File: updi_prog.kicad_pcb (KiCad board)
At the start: 2 copper layers, 50 x 37 mm, 17 parts, among them J1 UPDI, P1 USB_B, U1 LM1117-3.3, U2 FT232RL

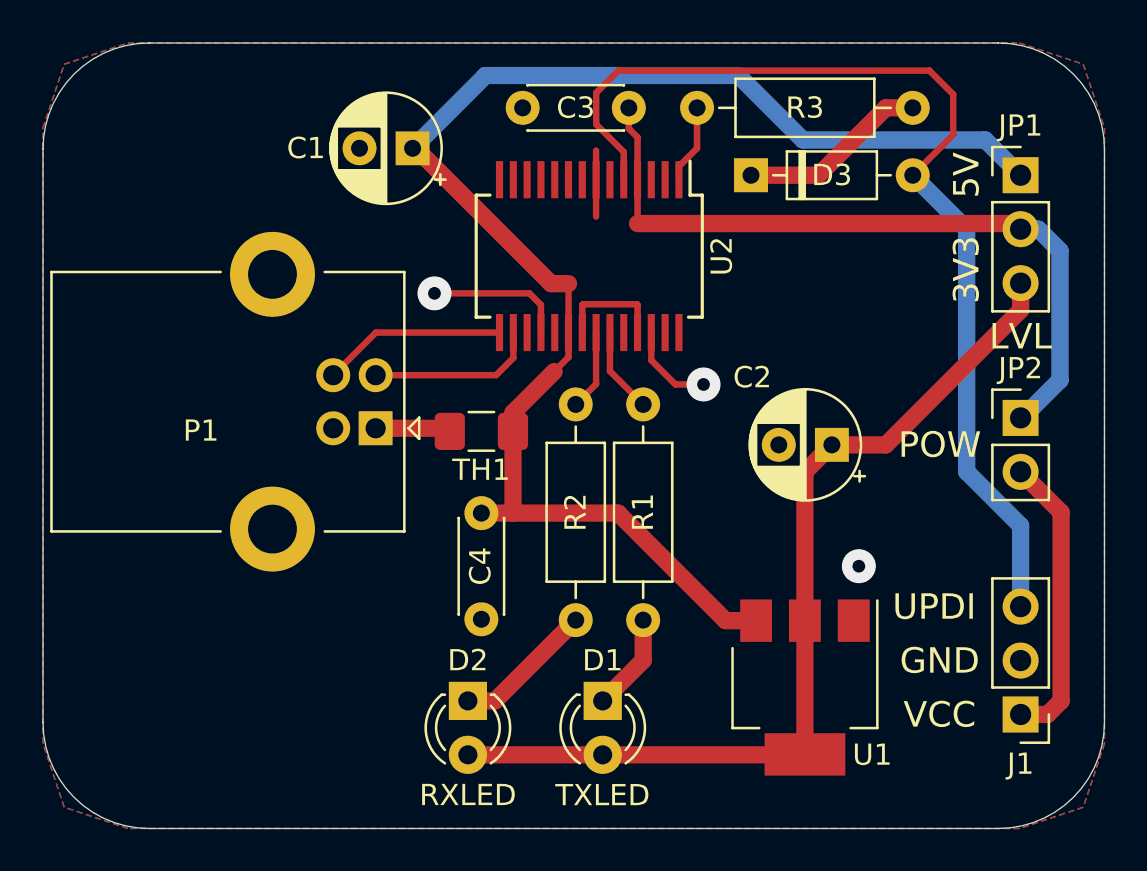
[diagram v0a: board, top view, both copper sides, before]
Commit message: added power led
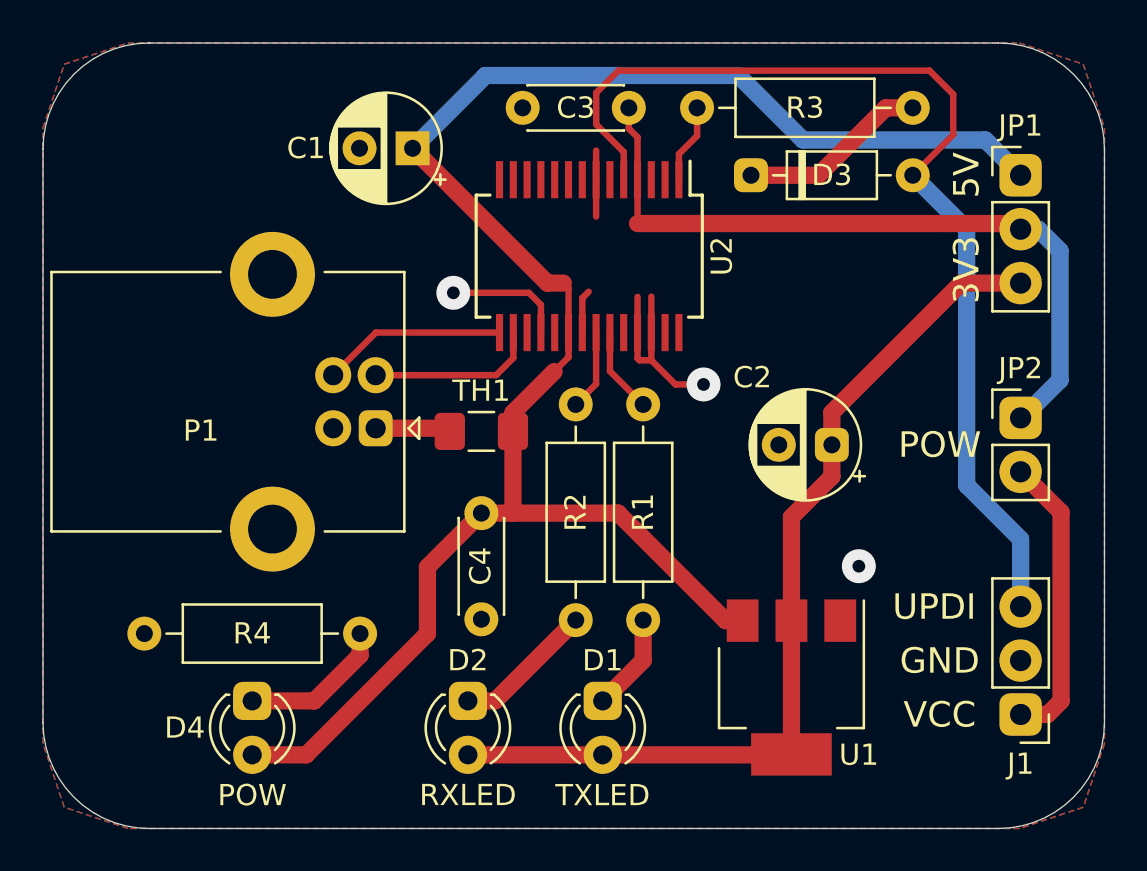
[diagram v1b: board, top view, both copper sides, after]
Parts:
- added D4: POW, LED_THT:LED_D3.0mm_Clear, F.Cu at (109.9, 87.0)
- added R4: 470, Resistor_THT:R_Axial_DIN0207_L6.3mm_D2.5mm_P10.16mm_Horizontal, F.Cu at (104.8, 83.8)
- moved U1 0.63 mm to (135.3, 86.4)
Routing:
- net VUSB: track 69.0 -> 85.5 mm
- net Net-(D4-Pad1): track 0.00 -> 6.99 mm
- net GND: track 19.1 -> 20.3 mm

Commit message: smaller pcb
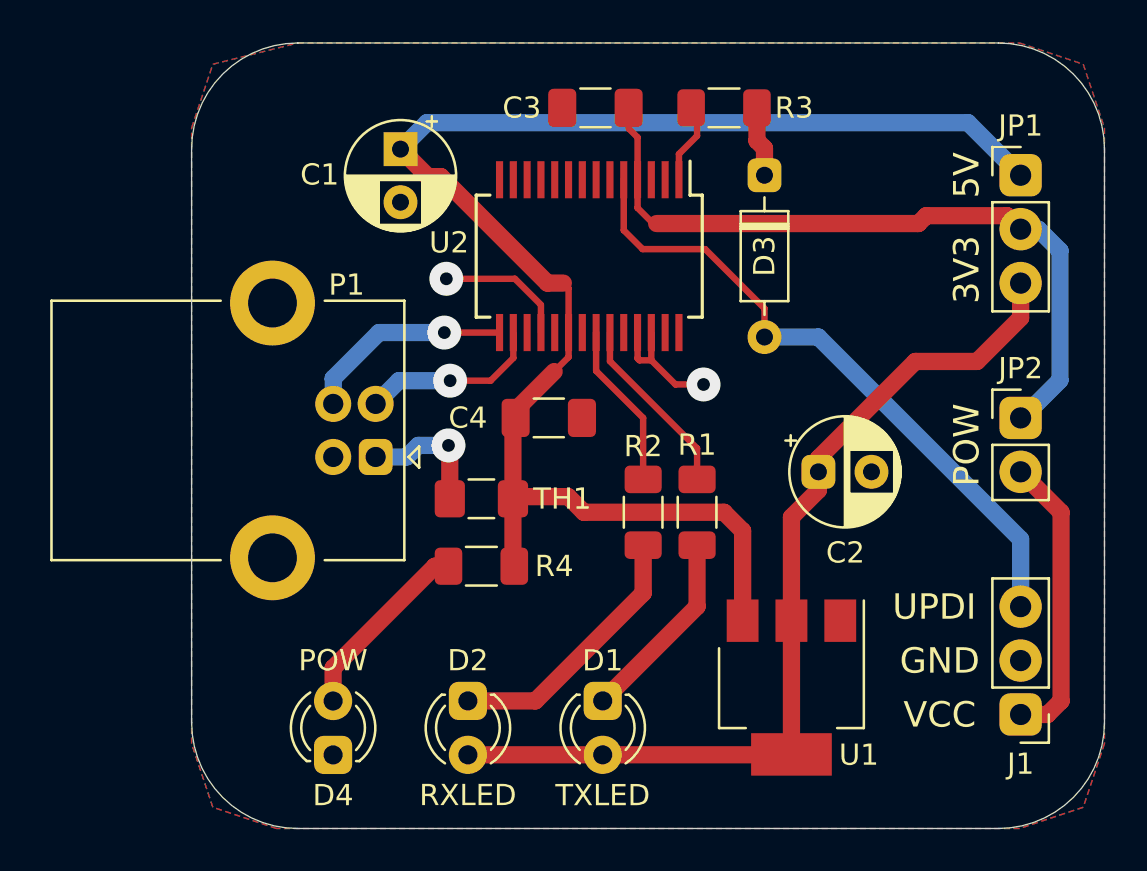
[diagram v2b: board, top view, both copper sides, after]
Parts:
- C1, C2: value 10u -> 22u
- C3, C4: footprint Capacitor_THT:C_Disc_D4.3mm_W1.9mm_P5.00mm -> Capacitor_SMD:C_1206_3216Metric_Pad1.33x1.80mm_HandSolder
- R1, R2, R3, R4: footprint Resistor_THT:R_Axial_DIN0207_L6.3mm_D2.5mm_P10.16mm_Horizontal -> Resistor_SMD:R_1206_3216Metric_Pad1.30x1.75mm_HandSolder
- moved R4 16.2 mm to (120.7, 80.6)
- moved R3 8.89 mm to (132.1, 59.1)
- moved R2 5.99 mm to (128.3, 78.1)
- moved R1 5.68 mm to (130.8, 78.1)
- moved C4 5.50 mm to (123.8, 73.7), turned to 0 degrees
- moved D4 4.58 mm to (113.7, 89.5), turned to 90 degrees
- moved TH1 3.17 mm to (120.7, 77.5)
- moved C3 1.57 mm to (126.0, 59.1)
- moved C2 1.42 mm to (136.5, 76.2), turned to 0 degrees
- moved P1 1.35 mm to (115.7, 75.5)
- moved D3 0.64 mm to (134.0, 62.2), turned to -90 degrees
- moved C1 0.57 mm to (116.8, 61.0), turned to -90 degrees
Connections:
- D4 pad 1: Net-(D4-Pad1) -> GND
- D4 pad 2: VUSB -> Net-(D4-Pad2)
- R4 pad 1: GND -> Net-(D4-Pad2)
- R4 pad 2: Net-(D4-Pad1) -> VUSB
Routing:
- net RX: track 49.4 -> 31.1 mm
- net VUSB: track 85.5 -> 71.3 mm
- net Net-(D4-Pad2): track 0.00 -> 8.97 mm
- net GND: track 20.3 -> 12.4 mm, vias 3 -> 2
- net Net-(D4-Pad1): track 6.99 -> 0.00 mm
- net Net-(D2-Pad1): track 6.66 -> 12.6 mm
- net Net-(D3-Pad1): track 8.94 -> 3.32 mm
- net Net-(R1-Pad1): track 4.03 -> 8.62 mm
- net Net-(D1-Pad1): track 4.59 -> 9.18 mm
- net Net-(R2-Pad1): track 3.78 -> 7.83 mm
- net Net-(P1-Pad1): track 3.55 -> 6.20 mm, vias 0 -> 1
- net D+: track 8.67 -> 9.93 mm, vias 0 -> 1
- net D-: track 8.02 -> 8.58 mm, vias 0 -> 1
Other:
- board size 50 x 37 mm -> 43 x 37 mm

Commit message: changed connector to standard AVR-UPDI
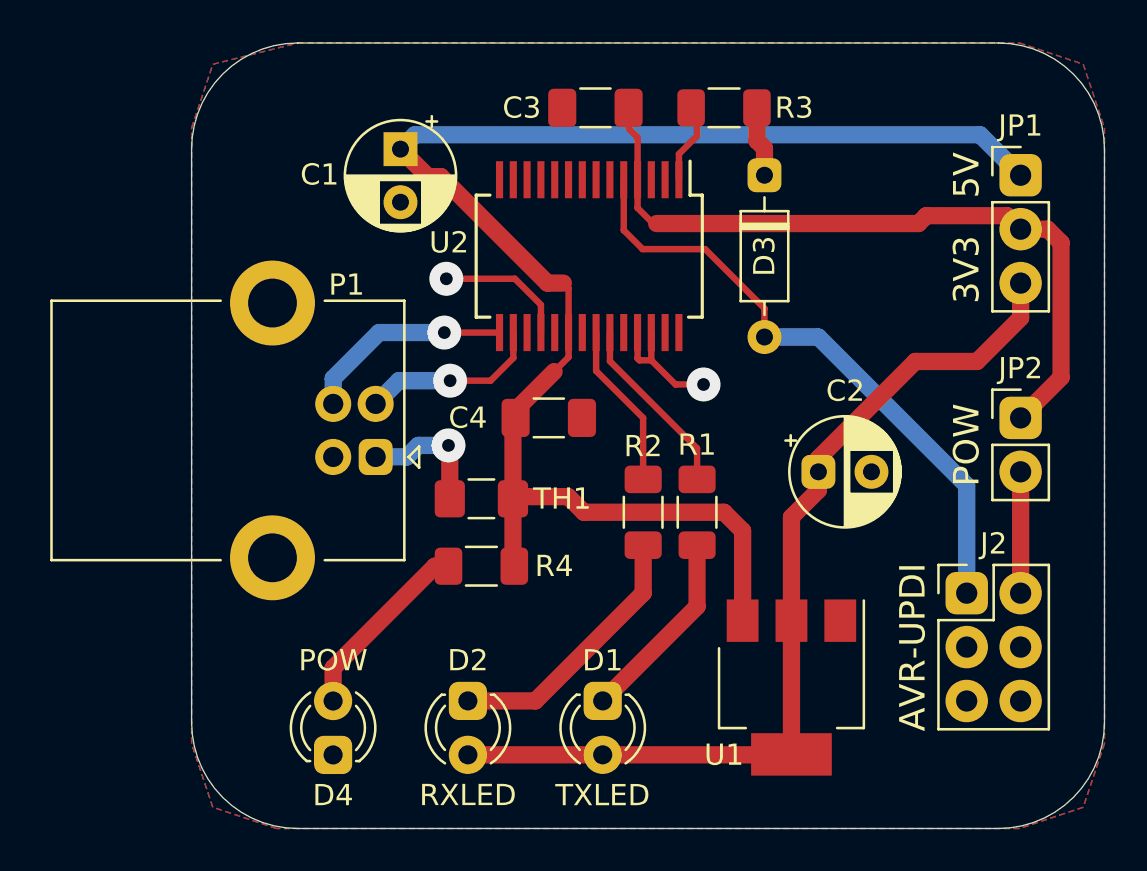
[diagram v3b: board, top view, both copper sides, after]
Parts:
- removed J1: UPDI, Connector_PinHeader_2.54mm:PinHeader_1x03_P2.54mm_Vertical
- added J2: AVR-UPDI-6, Connector_PinHeader_2.54mm:PinHeader_2x03_P2.54mm_Vertical, F.Cu at (143.5, 81.9)
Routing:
- net Net-(J2-Pad2): track 13.8 -> 5.72 mm
- net RX: track 31.1 -> 29.4 mm
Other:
- board text added: "AVR-UPDI"
- board text removed: "GND"
- board text removed: "UPDI"
- board text removed: "VCC"
